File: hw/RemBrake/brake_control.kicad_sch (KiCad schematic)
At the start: 25 parts, among them J6 Conn_01x07, J7 Conn_01x07, J8 Conn_01x03, Q10 BC337, Q11 BC847

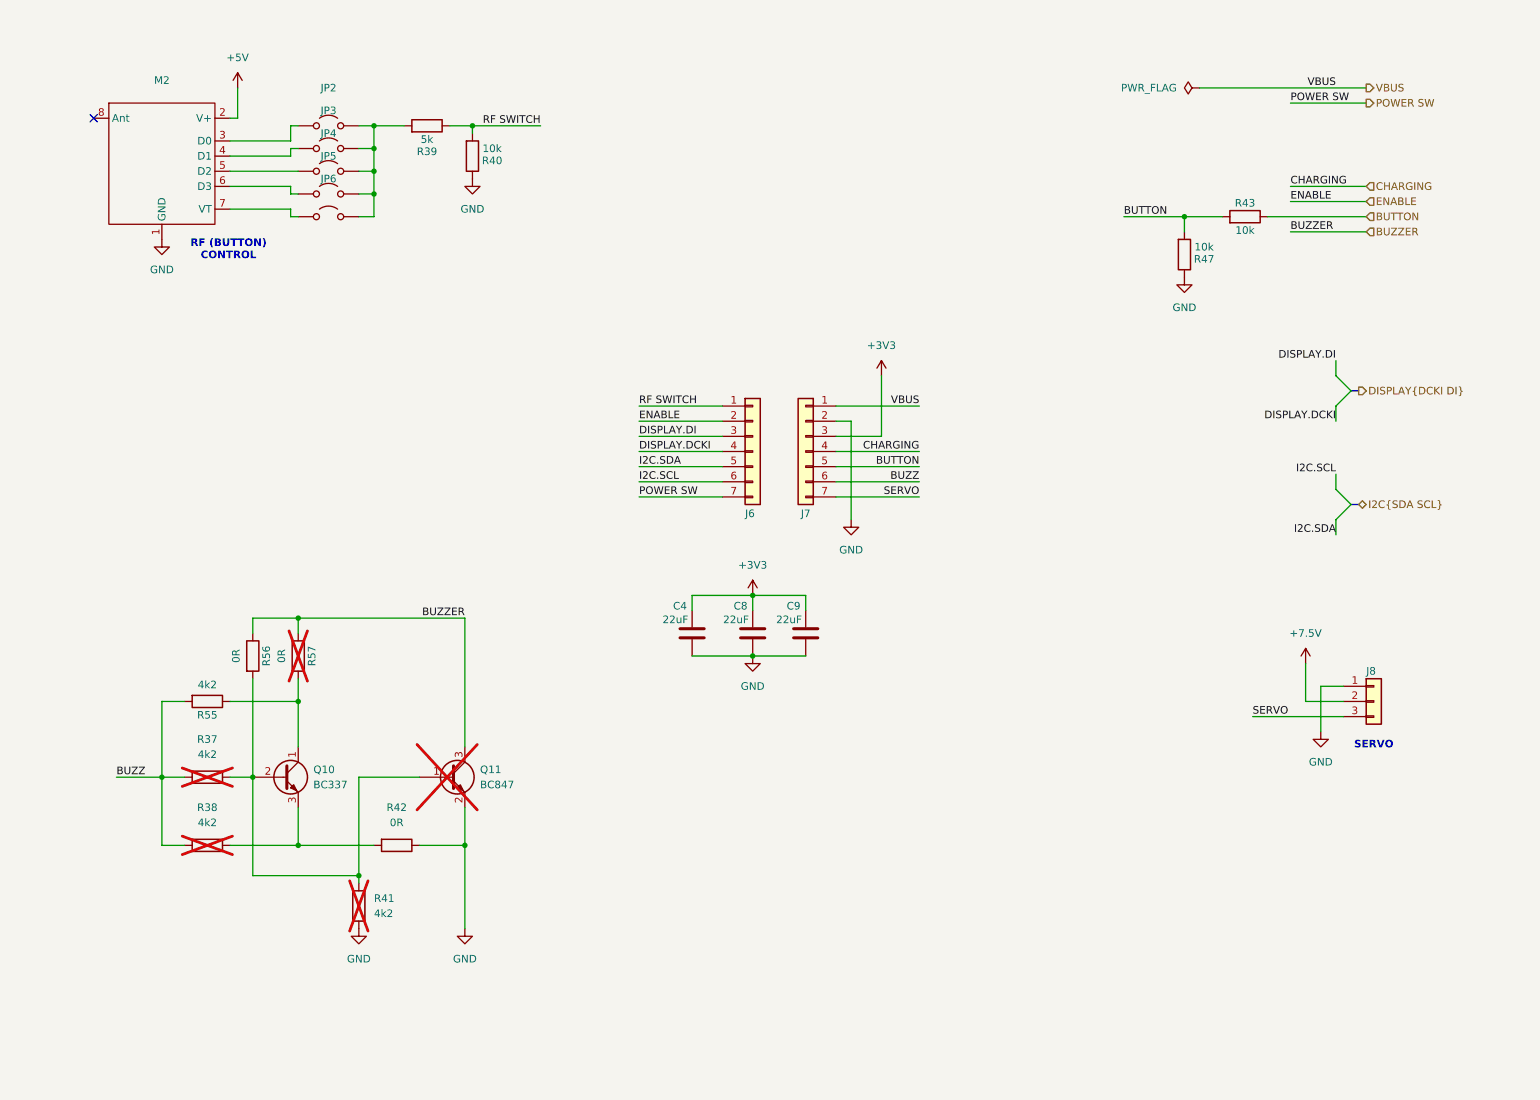
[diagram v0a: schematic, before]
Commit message: project renamed, schematics changed based on breakout boards notes and created new layout with better connectors
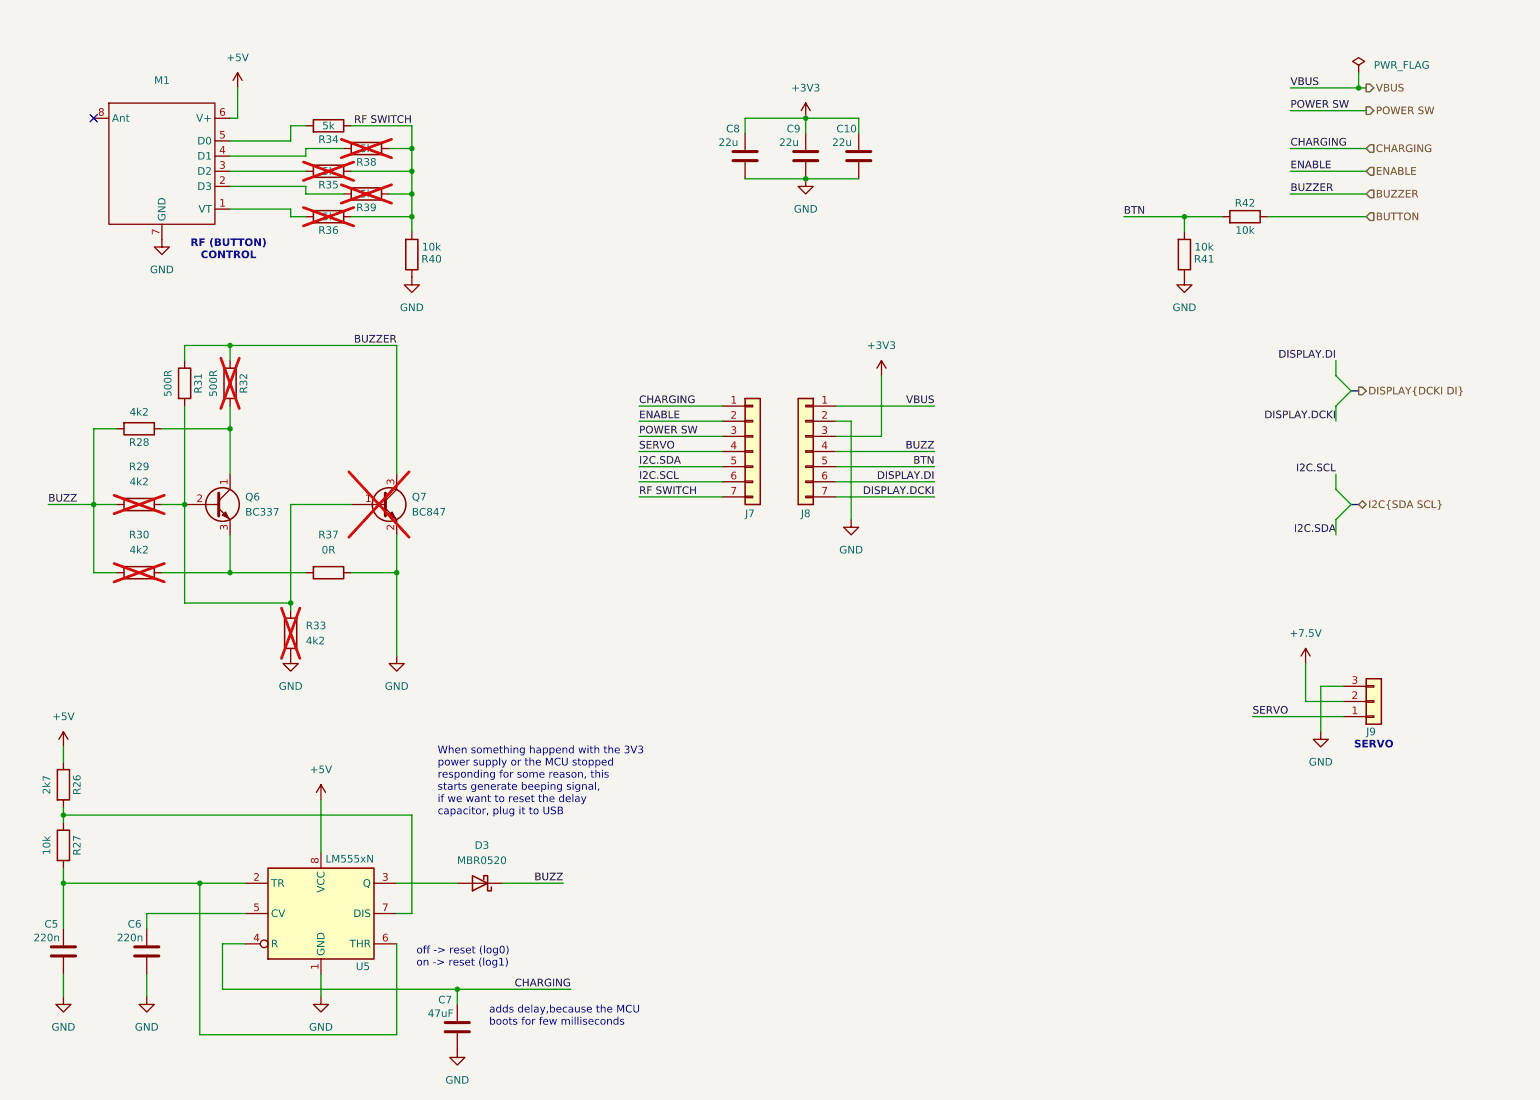
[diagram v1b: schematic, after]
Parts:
- removed JP2, JP3, JP4, JP5, JP6: Jumper_2_Open, symbol Jumper:Jumper_2_Open
- removed M2: ~, chinese_modules:RF_controller, symbol chinese_modules:RF_controller
- added C5, C6: 220n, Capacitor_SMD:C_0805_2012Metric_Pad1.18x1.45mm_HandSolder, symbol Device:C
- added C7: 47uF, Capacitor_SMD:C_0805_2012Metric_Pad1.18x1.45mm_HandSolder, symbol Device:C
- added D3: MBR0520, Diode_SMD:D_SOD-123, symbol Diode:MBR0520
- added M1: ~, chinese_modules:RF_controller, symbol chinese_modules:RF_controller
- added R26: 2k7, Resistor_SMD:R_0805_2012Metric_Pad1.20x1.40mm_HandSolder, symbol Device:R
- added R27: 10k, Resistor_SMD:R_0805_2012Metric_Pad1.20x1.40mm_HandSolder, symbol Device:R
- added R35, R36, R38, R39: 5k, Resistor_SMD:R_0805_2012Metric_Pad1.20x1.40mm_HandSolder, symbol Device:R
- added U5: LM555xN, Package_DIP:DIP-8_W7.62mm, symbol Timer:LM555xN
- C10: renamed from C9; value 22uF -> 22u
- C8: renamed from C4; value 22uF -> 22u
- C9: renamed from C8; value 22uF -> 22u
- R31: renamed from R56; value 0R -> 500R
- R32: renamed from R57; value 0R -> 500R
- renumbered J6 to J7, J7 to J8, J8 to J9, Q10 to Q6, Q11 to Q7, R55 to R28, R37 to R29, R38 to R30, R41 to R33, R39 to R34, R42 to R37, R47 to R41, R43 to R42
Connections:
- net +5V: now also M1.6 (V+), R26.1, U5.8 (VCC)
- net BUTTON: no longer J8.5 (Pin_5), R41.2, R42.2
- net BUZZ: now also J8.4 (Pin_4), D3.1 (K); no longer J8.6 (Pin_6)
- net CHARGING: now also J7.1 (Pin_1), C7.1, U5.4 (R); no longer J8.4 (Pin_4)
- net DISPLAY.DCKI: now also J8.7 (Pin_7); no longer J7.4 (Pin_4)
- net DISPLAY.DI: now also J8.6 (Pin_6); no longer J7.3 (Pin_3)
- net GND: now also J9.3 (Pin_3), C5.2, C6.2, C7.2, M1.7 (GND), U5.1 (GND); no longer J9.1 (Pin_1)
- net POWER SW: now also J7.3 (Pin_3); no longer J7.7 (Pin_7)
- net RF SWITCH: now also J7.7 (Pin_7), R35.1, R36.1, R38.1, R39.1; no longer J7.1 (Pin_1)
- net SERVO: now also J7.4 (Pin_4), J9.1 (Pin_1); no longer J8.7 (Pin_7), J9.3 (Pin_3)
- net at R34.2: now also M1.5 (D0)
- new net: M1.1 (VT), R36.2
- new net: M1.2 (D3), R39.2
- new net: M1.3 (D2), R35.2
- new net: M1.4 (D1), R38.2
- new net: D3.2 (A), U5.3 (Q)
- new net: C5.1, R27.2, U5.2 (TR), U5.6 (THR)
- new net: C6.1, U5.5 (CV)
- new net: R26.2, R27.1, U5.7 (DIS)
- new net BTN: J8.5 (Pin_5), R41.2, R42.2
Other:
- note added: "When something happend with the 3V3 power supply or the MCU stopped responding for some reason, this starts generate beeping signal, if we want to reset the delay capacitor, plug it to USB"
- note added: "adds delay,because the MCU boots for few milliseconds"
- note added: "off -> reset (log0) on -> reset (log1)"
- title: Break Control -> Brake Control
- moved on the sheet: C10, C8, C9, Q6, Q7, R28, R29, R30, R31, R32, R33, R34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

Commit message: added few components to fix indicator LED undefined cathode voltage and added vbus divider to match MCU voltage level
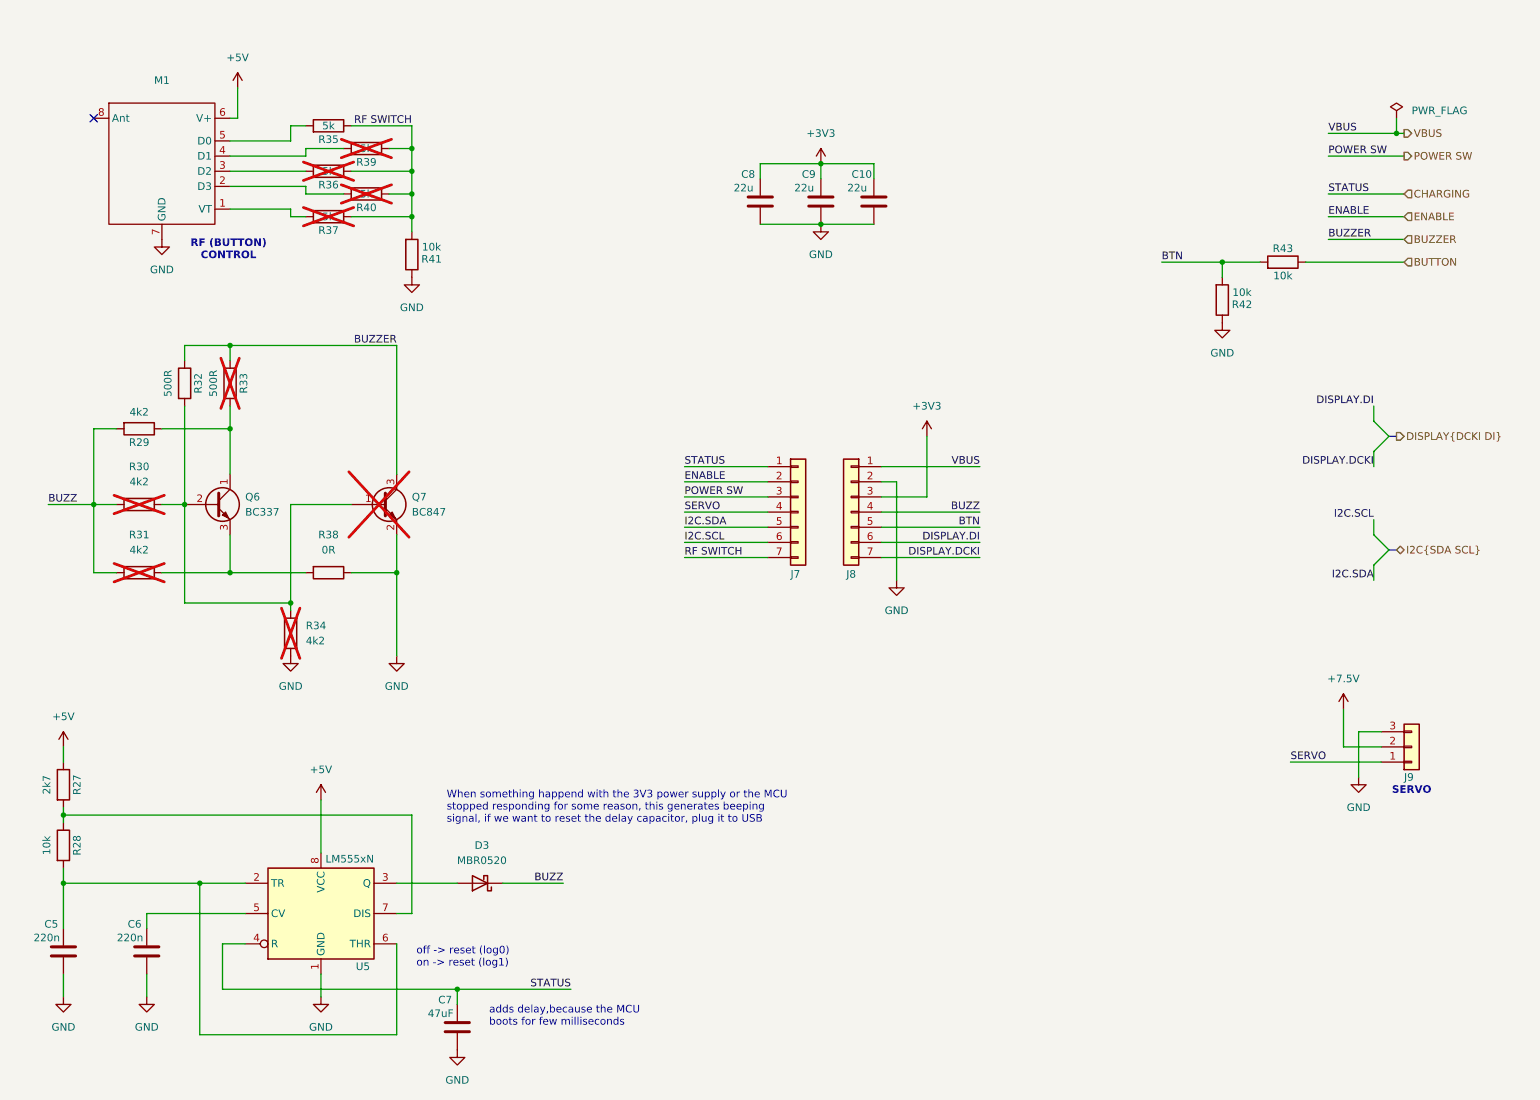
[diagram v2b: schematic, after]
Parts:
- renumbered R26 to R27, R27 to R28, R28 to R29, R29 to R30, R30 to R31, R31 to R32, R32 to R33, R33 to R34, R34 to R35, R35 to R36, R36 to R37, R37 to R38, R38 to R39, R39 to R40, R40 to R41, R41 to R42, R42 to R43
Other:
- note added: "When something happend with the 3V3 power supply or the MCU stopped responding for some reason, this generates beeping signal, if we want to reset the delay capacitor, plug it to USB"
- note removed: "When something happend with the 3V3 power supply or the MCU stopped responding for some reason, this starts generate beeping signal, if we want to reset the delay capacitor, plug it to USB"
- moved on the sheet: C10, C8, C9, J7, J8, J9, R42, R43

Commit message: updated date and revision in the schematics
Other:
- company: (none) -> Pacner Bros Tech
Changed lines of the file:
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@@
 	(title_block
 		(title "Brake Control")
-		(date "2024-12-15")
-		(rev "1.0")
+		(date "2025-02-23")
+		(rev "2.0")
+		(company "Pacner Bros Tech")
 	)
 	(bus_alias "DISPLAY"

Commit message: updated annotation
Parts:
- C10, C8, C9: value 22u -> 22uF
- C5, C6: value 220n -> 220nF
- Q7: now left out of the parts list
- R33: renamed from R29; value 4k2 -> 5k
- R34: renamed from R30; value 4k2 -> 5k; now left out of the parts list
- R35: renamed from R31; value 4k2 -> 5k; now left out of the parts list
- R36: renamed from R32; value 500R -> 200R
- R37: renamed from R33; value 500R -> 200R; now left out of the parts list
- R38: renamed from R34; value 4k2 -> 5k; now left out of the parts list
- R40: renamed from R36; now left out of the parts list
- R41: renamed from R37; now left out of the parts list
- R43: renamed from R39; now left out of the parts list
- R44: renamed from R40; now left out of the parts list
- R46: renamed from R42; value 10k -> 5k
- renumbered R27 to R31, R28 to R32, R35 to R39, R38 to R42, R41 to R45, R43 to R47

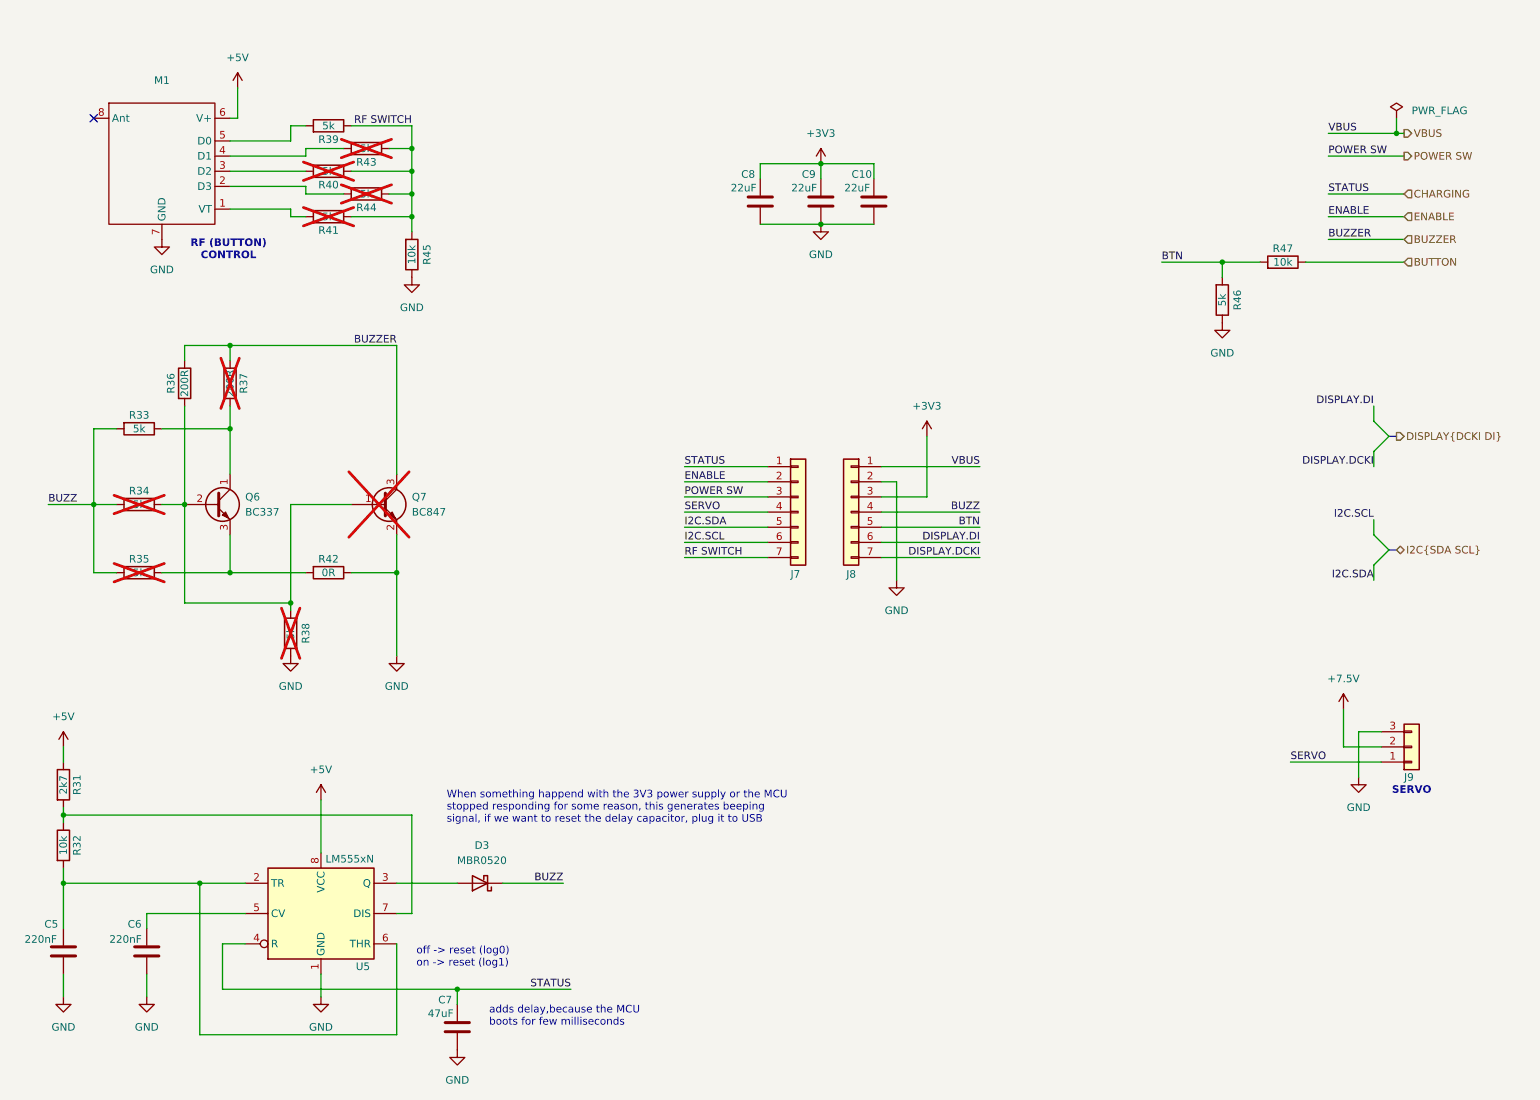
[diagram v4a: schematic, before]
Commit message: added 555 counter output divider to adjust to 3v3 voltage level
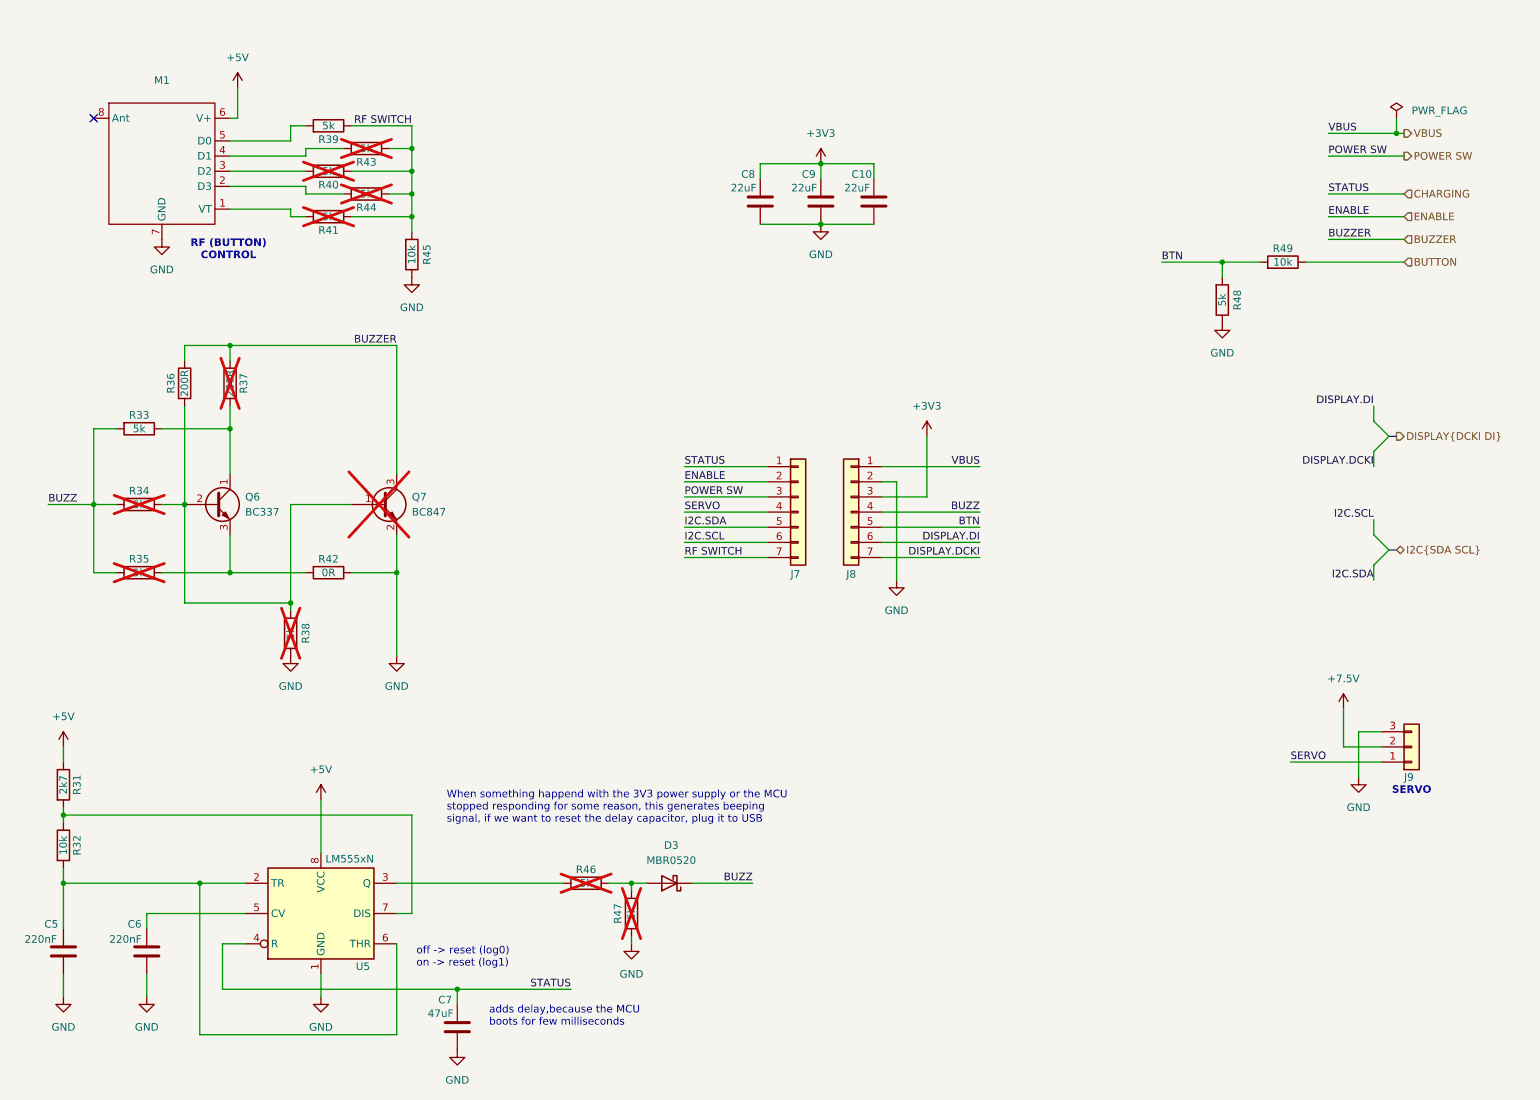
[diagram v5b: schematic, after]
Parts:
- added R46, R47: 5k, Resistor_SMD:R_0805_2012Metric_Pad1.20x1.40mm_HandSolder, symbol Device:R
- renumbered R46 to R48, R47 to R49
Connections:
- net GND: now also R47.1
- net at D3.2 (A): now also R46.2, R47.2; no longer U5.3 (Q)
- new net: R46.1, U5.3 (Q)
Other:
- moved on the sheet: D3
